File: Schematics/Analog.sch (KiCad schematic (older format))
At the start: 27 parts, among them P4 CONN_7X2, U3 RESISTOR_ARRAY, U7 AD7193, U8 AS1359-3

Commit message: Moved the .kicad_pcb file to the board folder. Also did some more routing.
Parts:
- C20, C26, C27, C28, C29, C30, C31, C32, C33, C34, C35, C36, C37, C38, C39: footprint 0805 -> c_0805
- P4: footprint (none) -> pinhead-2X07
- R18, R21, R25, R26, R27, R28, R29, R30: footprint 0805 -> SM0805
- U3: footprint SOIC-16 -> SOIC-16_Narrow_RearrangedPins
- U7: footprint 28-TSSOP -> dp_devices-TSSOP-28
- U8: footprint TOST23-5 -> dp_devices-SOT-23-5

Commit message: Found out that there are two different remappable pins of the dsPIC33E. Some are input/out remappable and some are input only remappable. Fixed the XBee SPI, XBEE nRESET, and Green LED on the RGB LED to make sure they are all outputs.
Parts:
- added P14: CONN_4X2, symbol CONN_4X2
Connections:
- wire segments 96 -> 106
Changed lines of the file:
@@
 LIBS:contrib
 LIBS:valves
+LIBS:TPS2113A
 LIBS:sn65hvd232
+LIBS:Si1970DH
+LIBS:RGB_LED
+LIBS:RESISTOR_ARRAY
+LIBS:pinhead
+LIBS:MPU-9150
+LIBS:MPU-6000_MPU-6050
+LIBS:microchip_can
+LIBS:MAG3110
+LIBS:DSPIC33E128MC506
+LIBS:dp_devices
+LIBS:AS1359
+LIBS:AP7363
+LIBS:AD7193
 LIBS:AD7192
-LIBS:AS1359
-LIBS:AD7193
-LIBS:DSPIC33E128MC506
-LIBS:AP7363
-LIBS:MPU-6000_MPU-6050
-LIBS:TPS2113A
-LIBS:MPU-9150
-LIBS:RGB_LED
-LIBS:Si1970DH
-LIBS:MAG3110
-LIBS:RESISTOR_ARRAY
-LIBS:con-commcon
-LIBS:pinhead
 LIBS:sw_push_4
 LIBS:Sensor_Board-cache
@@
 AIN8
 Text Label 5800 5350 0    60   ~ 0
+REFIN1+
+Text Label 6950 5350 0    60   ~ 0
+REFIN1-
+Text Label 5800 5250 0    60   ~ 0
 REFIN2+
-Text Label 6950 5350 0    60   ~ 0
+Text Label 6950 5250 0    60   ~ 0
 REFIN2-
-Text Label 5800 5250 0    60   ~ 0
-REFIN1+
-Text Label 6950 5250 0    60   ~ 0
-REFIN1-
 NoConn ~ 4600 2200
 NoConn ~ 4600 2500
@@
 	1    0    0    -1
 $EndComp
+$Comp
+L CONN_4X2 P14
+U 1 1 51FB0AF2
+P 5600 6000
+F 0 "P14" H 5600 6250 50  0000 C CNN
+F 1 "CONN_4X2" V 5600 6000 40  0000 C CNN
+F 2 "" H 5600 6000 60  0000 C CNN
+F 3 "" H 5600 6000 60  0000 C CNN
+	1    5600 6000
+	1    0    0    -1
+$EndComp
+$Comp
+L VAA #PWR083
+U 1 1 51FB0AFF
+P 6100 5750
+F 0 "#PWR083" H 6100 5810 30  0001 C CNN
+F 1 "VAA" H 6100 5860 30  0000 C CNN
+F 2 "" H 6100 5750 60  0001 C CNN
+F 3 "" H 6100 5750 60  0001 C CNN
+	1    6100 5750
+	1    0    0    -1
+$EndComp
+$Comp
+L AGND #PWR084
+U 1 1 51FB0B05
+P 5050 6200
+F 0 "#PWR084" H 5050 6200 40  0001 C CNN
+F 1 "AGND" H 5050 6130 50  0000 C CNN
+F 2 "" H 5050 6200 60  0001 C CNN
+F 3 "" H 5050 6200 60  0001 C CNN
+	1    5050 6200
+	1    0    0    -1
+$EndComp
 Wire Wire Line
 	3050 3150 3050 2950
@@
 Wire Wire Line
 	3650 3200 3850 3200
+Wire Wire Line
+	5200 5850 5050 5850
+Wire Wire Line
+	5050 5850 5050 6200
+Wire Wire Line
+	5200 5950 5050 5950
+Connection ~ 5050 5950
+Wire Wire Line
+	5200 6050 5050 6050
+Connection ~ 5050 6050
+Wire Wire Line
+	5200 6150 5050 6150
+Connection ~ 5050 6150
+Wire Wire Line
+	6000 6150 6100 6150
+Wire Wire Line
+	6100 6150 6100 5750
+Wire Wire Line
+	6000 6050 6100 6050
+Connection ~ 6100 6050
+Wire Wire Line
+	6000 5950 6100 5950
+Connection ~ 6100 5950
+Wire Wire Line
+	6000 5850 6100 5850
+Connection ~ 6100 5850
 $EndSCHEMATC

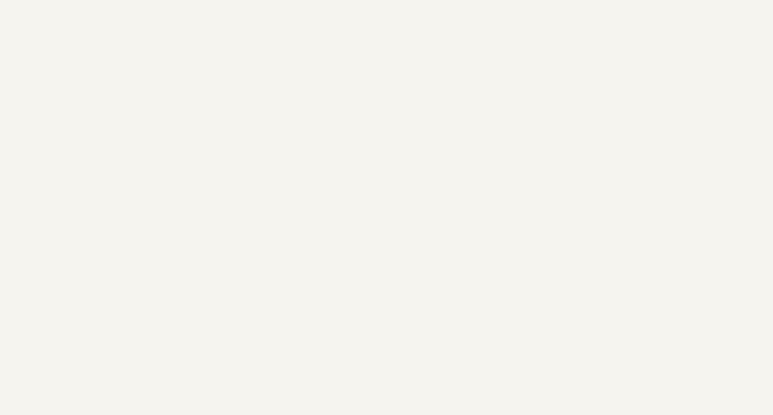
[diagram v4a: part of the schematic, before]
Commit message: Changed the Mounting holes to accept M3 screws
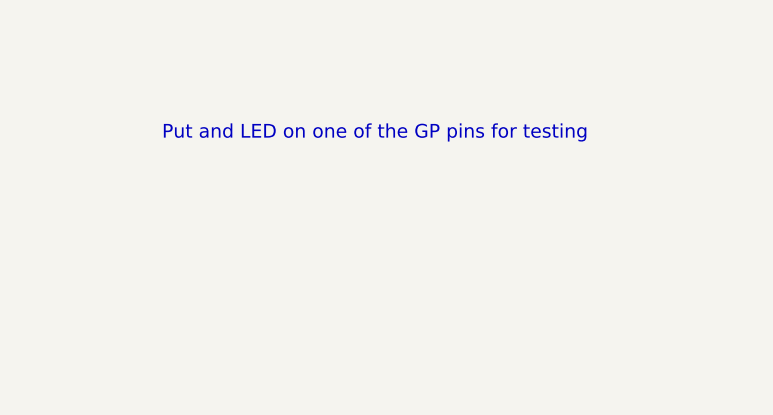
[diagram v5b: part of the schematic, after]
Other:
- note added: "Put and LED on one of the GP pins for testing\n"
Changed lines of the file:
@@
 	6000 5850 6100 5850
 Connection ~ 6100 5850
+Text Notes 8500 900  0    60   ~ 0
+Put and LED on one of the GP pins for testing\n
 $EndSCHEMATC

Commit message: Updated to version 1.2
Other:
- note added: "-Put and LED on one of the GP pins for testing\n-Breakout SPI Pins\n-Change configuration for both full and half sensing. Attach AINCOM.\n"
- note removed: "Put and LED on one of the GP pins for testing\n"
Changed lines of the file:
@@
 REFIN1+
 $Comp
-L AGND #PWR061
+L AGND #PWR062
 U 1 1 51E814BF
 P 5600 1000
-F 0 "#PWR061" H 5600 1000 40  0001 C CNN
+F 0 "#PWR062" H 5600 1000 40  0001 C CNN
 F 1 "AGND" H 5600 930 50  0000 C CNN
 F 2 "" H 5600 1000 60  0001 C CNN
@@
 $EndComp
 $Comp
-L PWR_FLAG #FLG062
+L PWR_FLAG #FLG063
 U 1 1 51E814BE
 P 5600 900
-F 0 "#FLG062" H 5600 995 30  0001 C CNN
+F 0 "#FLG063" H 5600 995 30  0001 C CNN
 F 1 "PWR_FLAG" H 5600 1080 30  0000 C CNN
 F 2 "" H 5600 900 60  0001 C CNN
@@
 Analog Sensors and Power
 $Comp
-L VAA #PWR063
+L VAA #PWR064
 U 1 1 51E814BD
 P 7000 2500
-F 0 "#PWR063" H 7000 2560 30  0001 C CNN
+F 0 "#PWR064" H 7000 2560 30  0001 C CNN
 F 1 "VAA" H 7000 2610 30  0000 C CNN
 F 2 "" H 7000 2500 60  0001 C CNN
@@
 $EndComp
 $Comp
-L VAA #PWR064
+L VAA #PWR065
 U 1 1 51E814BC
 P 7200 2300
-F 0 "#PWR064" H 7200 2360 30  0001 C CNN
+F 0 "#PWR065" H 7200 2360 30  0001 C CNN
 F 1 "VAA" H 7200 2410 30  0000 C CNN
 F 2 "" H 7200 2300 60  0001 C CNN
@@
 $EndComp
 $Comp
-L VAA #PWR065
+L VAA #PWR066
 U 1 1 51E814B8
 P 6550 4000
-F 0 "#PWR065" H 6550 4060 30  0001 C CNN
+F 0 "#PWR066" H 6550 4060 30  0001 C CNN
 F 1 "VAA" H 6550 4110 30  0000 C CNN
 F 2 "" H 6550 4000 60  0001 C CNN
@@
 $EndComp
 $Comp
-L VAA #PWR066
+L VAA #PWR067
 U 1 1 51E814B7
 P 5350 950
-F 0 "#PWR066" H 5350 1010 30  0001 C CNN
+F 0 "#PWR067" H 5350 1010 30  0001 C CNN
 F 1 "VAA" H 5350 1060 30  0000 C CNN
 F 2 "" H 5350 950 60  0001 C CNN
@@
 $EndComp
 $Comp
-L PWR_FLAG #FLG067
+L PWR_FLAG #FLG068
 U 1 1 51E814B6
 P 5350 900
-F 0 "#FLG067" H 5350 995 30  0001 C CNN
+F 0 "#FLG068" H 5350 995 30  0001 C CNN
 F 1 "PWR_FLAG" H 5350 1080 30  0000 C CNN
 F 2 "" H 5350 900 60  0001 C CNN
@@
 $EndComp
 $Comp
-L +3.3V #PWR068
+L +3.3V #PWR069
 U 1 1 51E814B4
 P 4400 3800
-F 0 "#PWR068" H 4400 3760 30  0001 C CNN
+F 0 "#PWR069" H 4400 3760 30  0001 C CNN
 F 1 "+3.3V" H 4400 3910 30  0000 C CNN
 F 2 "" H 4400 3800 60  0001 C CNN
@@
 REFIN2-
 $Comp
-L VAA #PWR069
+L VAA #PWR070
 U 1 1 51E814B1
 P 7100 3000
-F 0 "#PWR069" H 7100 3060 30  0001 C CNN
+F 0 "#PWR070" H 7100 3060 30  0001 C CNN
 F 1 "VAA" H 7100 3110 30  0000 C CNN
 F 2 "" H 7100 3000 60  0001 C CNN
@@
 REFIN1+
 $Comp
-L +3.3V #PWR070
+L +3.3V #PWR071
 U 1 1 51E814B0
 P 7300 2350
-F 0 "#PWR070" H 7300 2310 30  0001 C CNN
+F 0 "#PWR071" H 7300 2310 30  0001 C CNN
 F 1 "+3.3V" H 7300 2460 30  0000 C CNN
 F 2 "" H 7300 2350 60  0001 C CNN
@@
 $EndComp
 $Comp
-L AGND #PWR071
+L AGND #PWR072
 U 1 1 51E814AF
 P 6500 4400
-F 0 "#PWR071" H 6500 4400 40  0001 C CNN
+F 0 "#PWR072" H 6500 4400 40  0001 C CNN
 F 1 "AGND" H 6500 4330 50  0000 C CNN
 F 2 "" H 6500 4400 60  0001 C CNN
@@
 $EndComp
 $Comp
-L AGND #PWR072
+L AGND #PWR073
 U 1 1 51E814AE
 P 7250 2750
-F 0 "#PWR072" H 7250 2750 40  0001 C CNN
+F 0 "#PWR073" H 7250 2750 40  0001 C CNN
 F 1 "AGND" H 7250 2680 50  0000 C CNN
 F 2 "" H 7250 2750 60  0001 C CNN
@@
 $EndComp
 $Comp
-L GND #PWR073
+L GND #PWR074
 U 1 1 51E814AD
 P 7350 2650
-F 0 "#PWR073" H 7350 2650 30  0001 C CNN
+F 0 "#PWR074" H 7350 2650 30  0001 C CNN
 F 1 "GND" H 7350 2580 30  0001 C CNN
 F 2 "" H 7350 2650 60  0001 C CNN
@@
 $EndComp
 $Comp
-L AGND #PWR074
+L AGND #PWR075
 U 1 1 51F0BE65
 P 3850 3700
-F 0 "#PWR074" H 3850 3700 40  0001 C CNN
+F 0 "#PWR075" H 3850 3700 40  0001 C CNN
 F 1 "AGND" H 3850 3630 50  0000 C CNN
 F 2 "" H 3850 3700 60  0001 C CNN
@@
 $EndComp
 $Comp
-L AGND #PWR075
+L AGND #PWR076
 U 1 1 51F0BE6B
 P 3750 3600
-F 0 "#PWR075" H 3750 3600 40  0001 C CNN
+F 0 "#PWR076" H 3750 3600 40  0001 C CNN
 F 1 "AGND" H 3750 3530 50  0000 C CNN
 F 2 "" H 3750 3600 60  0001 C CNN
@@
 $EndComp
 $Comp
-L AGND #PWR076
+L AGND #PWR077
 U 1 1 51F0BE71
 P 3650 3500
-F 0 "#PWR076" H 3650 3500 40  0001 C CNN
+F 0 "#PWR077" H 3650 3500 40  0001 C CNN
 F 1 "AGND" H 3650 3430 50  0000 C CNN
 F 2 "" H 3650 3500 60  0001 C CNN
@@
 $EndComp
 $Comp
-L AGND #PWR077
+L AGND #PWR078
 U 1 1 51F0BE77
 P 3550 3400
-F 0 "#PWR077" H 3550 3400 40  0001 C CNN
+F 0 "#PWR078" H 3550 3400 40  0001 C CNN
 F 1 "AGND" H 3550 3330 50  0000 C CNN
 F 2 "" H 3550 3400 60  0001 C CNN
@@
 $EndComp
 $Comp
-L AGND #PWR078
+L AGND #PWR079
 U 1 1 51F0BE7D
 P 7250 3700
-F 0 "#PWR078" H 7250 3700 40  0001 C CNN
+F 0 "#PWR079" H 7250 3700 40  0001 C CNN
 F 1 "AGND" H 7250 3630 50  0000 C CNN
 F 2 "" H 7250 3700 60  0001 C CNN
@@
 $EndComp
 $Comp
-L AGND #PWR079
+L AGND #PWR080
 U 1 1 51F0BE83
 P 7350 3600
-F 0 "#PWR079" H 7350 3600 40  0001 C CNN
+F 0 "#PWR080" H 7350 3600 40  0001 C CNN
 F 1 "AGND" H 7350 3530 50  0000 C CNN
 F 2 "" H 7350 3600 60  0001 C CNN
@@
 $EndComp
 $Comp
-L AGND #PWR080
+L AGND #PWR081
 U 1 1 51F0BE89
 P 7450 3500
-F 0 "#PWR080" H 7450 3500 40  0001 C CNN
+F 0 "#PWR081" H 7450 3500 40  0001 C CNN
 F 1 "AGND" H 7450 3430 50  0000 C CNN
 F 2 "" H 7450 3500 60  0001 C CNN
@@
 $EndComp
 $Comp
-L AGND #PWR081
+L AGND #PWR082
 U 1 1 51F0BE8F
 P 7550 3400
-F 0 "#PWR081" H 7550 3400 40  0001 C CNN
+F 0 "#PWR082" H 7550 3400 40  0001 C CNN
 F 1 "AGND" H 7550 3330 50  0000 C CNN
 F 2 "" H 7550 3400 60  0001 C CNN
@@
 $EndComp
 $Comp
-L GND #PWR082
+L GND #PWR083
 U 1 1 51F0C1CD
 P 4400 4200
-F 0 "#PWR082" H 4400 4200 30  0001 C CNN
+F 0 "#PWR083" H 4400 4200 30  0001 C CNN
 F 1 "GND" H 4400 4130 30  0001 C CNN
 F 2 "" H 4400 4200 60  0001 C CNN
@@
 $EndComp
 $Comp
-L VAA #PWR083
+L VAA #PWR084
 U 1 1 51FB0AFF
 P 6100 5750
-F 0 "#PWR083" H 6100 5810 30  0001 C CNN
+F 0 "#PWR084" H 6100 5810 30  0001 C CNN
 F 1 "VAA" H 6100 5860 30  0000 C CNN
 F 2 "" H 6100 5750 60  0001 C CNN
@@
 $EndComp
 $Comp
-L AGND #PWR084
+L AGND #PWR085
 U 1 1 51FB0B05
 P 5050 6200
-F 0 "#PWR084" H 5050 6200 40  0001 C CNN
+F 0 "#PWR085" H 5050 6200 40  0001 C CNN
 F 1 "AGND" H 5050 6130 50  0000 C CNN
 F 2 "" H 5050 6200 60  0001 C CNN
@@
 	6000 5850 6100 5850
 Connection ~ 6100 5850
-Text Notes 8500 900  0    60   ~ 0
-Put and LED on one of the GP pins for testing\n
+Text Notes 3100 6650 0    118  ~ 0
+-Put and LED on one of the GP pins for testing\n-Breakout SPI Pins\n-Change configuration for both full and half sensing. Attach AINCOM.\n
 $EndSCHEMATC

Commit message: Started making changes to the Sensor Board for v.2
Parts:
- removed U3: RESISTOR_ARRAY, SOIC-16_Narrow_RearrangedPins, symbol RESISTOR_ARRAY
- C32: value 10uF -> 10nF
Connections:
- wire segments 106 -> 90
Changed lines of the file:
@@
 LIBS:contrib
 LIBS:valves
+LIBS:AD7192
+LIBS:AD7193
+LIBS:AP7363
+LIBS:AS1359
+LIBS:dp_devices
+LIBS:DSPIC33E128MC506
+LIBS:MAG3110
+LIBS:microchip_can
+LIBS:MPU-6000_MPU-6050
+LIBS:MPU-9150
+LIBS:pinhead
+LIBS:RESISTOR_ARRAY
+LIBS:RGB_LED
+LIBS:Si1970DH
+LIBS:sn65hvd232
+LIBS:sw_push_4
 LIBS:TPS2113A
-LIBS:sn65hvd232
-LIBS:Si1970DH
-LIBS:RGB_LED
-LIBS:RESISTOR_ARRAY
-LIBS:pinhead
-LIBS:MPU-9150
-LIBS:MPU-6000_MPU-6050
-LIBS:microchip_can
-LIBS:MAG3110
-LIBS:DSPIC33E128MC506
-LIBS:dp_devices
-LIBS:AS1359
-LIBS:AP7363
-LIBS:AD7193
-LIBS:AD7192
-LIBS:sw_push_4
+LIBS:microclasp_hdrx2
+LIBS:microclasp_hdrx3
 LIBS:Sensor_Board-cache
-EELAYER 24 0
+EELAYER 27 0
 EELAYER END
 $Descr A4 11693 8268
@@
 Sheet 2 3
 Title ""
-Date "19 jul 2013"
+Date "31 dec 2013"
 Rev ""
 Comp ""
@@
 P 6400 4100
 F 0 "C32" H 6400 4050 30  0000 L CNN
-F 1 "10uF" H 6400 4150 30  0000 L CNN
+F 1 "10nF" H 6400 4150 30  0000 L CNN
 F 2 "c_0805" H 6400 4100 60  0001 C CNN
 F 3 "" H 6400 4100 60  0001 C CNN
@@
 Text Label 8000 3100 1    60   ~ 0
 AIN8
-Text Label 3850 5400 0    60   ~ 0
-AIN7
-Text Label 3850 5300 0    60   ~ 0
-AIN7
-Text Label 3850 5200 0    60   ~ 0
-AIN5
-Text Label 3850 5100 0    60   ~ 0
-AIN5
-Text Label 3850 5000 0    60   ~ 0
-AIN3
-Text Label 3850 4900 0    60   ~ 0
-AIN3
-Text Label 3850 4800 0    60   ~ 0
-AIN1
-Text Label 3850 4700 0    60   ~ 0
-AIN1
-Text Label 5100 5400 0    60   ~ 0
-REFIN1-
-Text Label 5100 5200 0    60   ~ 0
-REFIN1-
-Text Label 5100 5000 0    60   ~ 0
-REFIN1-
-Text Label 5100 4800 0    60   ~ 0
-REFIN1-
-Text Label 5100 5300 0    60   ~ 0
-REFIN1+
-Text Label 5100 5100 0    60   ~ 0
-REFIN1+
-Text Label 5100 4900 0    60   ~ 0
-REFIN1+
-Text Label 5100 4700 0    60   ~ 0
-REFIN1+
 $Comp
 L AGND #PWR062
@@
 NoConn ~ 4600 3000
 $Comp
-L RESISTOR_ARRAY U3
-U 1 1 51E814AB
-P 4600 5050
-F 0 "U3" H 4400 5500 50  0000 C CNN
-F 1 "RESISTOR_ARRAY" H 4600 4600 50  0000 C CNN
-F 2 "SOIC-16_Narrow_RearrangedPins" H 4600 5050 50  0001 C CNN
-F 3 "DOCUMENTATION" H 4600 5050 50  0001 C CNN
-F 4 "3.96" H 4600 5050 60  0001 C CNN "Price"
-F 5 "Digikey" H 4600 5050 60  0001 C CNN "Retailer"
-F 6 "987-1076-ND" H 4600 5050 60  0001 C CNN "Part_Number"
-	1    4600 5050
-	1    0    0    -1
-$EndComp
-$Comp
 L AGND #PWR075
 U 1 1 51F0BE65
@@
 	6500 2900 7000 2900
 Wire Wire Line
-	4150 5300 3800 5300
-Wire Wire Line
-	4150 5100 3800 5100
-Wire Wire Line
-	4150 4900 3800 4900
-Wire Wire Line
-	4150 4700 3800 4700
-Wire Wire Line
-	5050 5300 5350 5300
-Wire Wire Line
-	5050 5100 5350 5100
-Wire Wire Line
-	5050 4900 5350 4900
-Wire Wire Line
-	5050 4700 5350 4700
-Wire Wire Line
 	6900 5350 7200 5350
 Wire Wire Line
@@
 	5600 900  5600 1000
 Wire Wire Line
-	5050 4800 5350 4800
-Wire Wire Line
-	5350 5000 5050 5000
-Wire Wire Line
-	5050 5200 5350 5200
-Wire Wire Line
-	5050 5400 5350 5400
-Wire Wire Line
-	4150 4800 3800 4800
-Wire Wire Line
-	4150 5000 3800 5000
-Wire Wire Line
-	4150 5200 3800 5200
-Wire Wire Line
-	4150 5400 3800 5400
-Wire Wire Line
 	3550 3300 3550 3400

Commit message: Continuing changes for v2
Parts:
- removed P14: CONN_4X2, symbol CONN_4X2
- removed P4: CONN_7X2, pinhead-2X07, symbol CONN_7X2
- added D?: LED, ~, symbol LED
- added J? (x8): MICROCLASP_HDRX3, symbol MICROCLASP_HDRX3
- added L?: F-BEAD, 0805, symbol INDUCTOR
- added R? (x2): 1k, SM0805, symbol R
- added R?: 200, SM0805, symbol R
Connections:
- wire segments 90 -> 124
- no-connect marks 5 -> 3
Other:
- note removed: "-Put and LED on one of the GP pins for testing\n-Breakout SPI Pins\n-Change configuration for both full and half sensing. Attach AINCOM.\n"
